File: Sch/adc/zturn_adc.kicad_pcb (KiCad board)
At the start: 4 copper layers, 91.5 x 80 mm, 118 parts, among them CN1 SMA, CN2 SMA, CN3 AudioJack, J1 JP4, J2 Header5, J3 JP2, J4 JP2, J5 JP2, J6 JP2, P1 CONN_02X40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

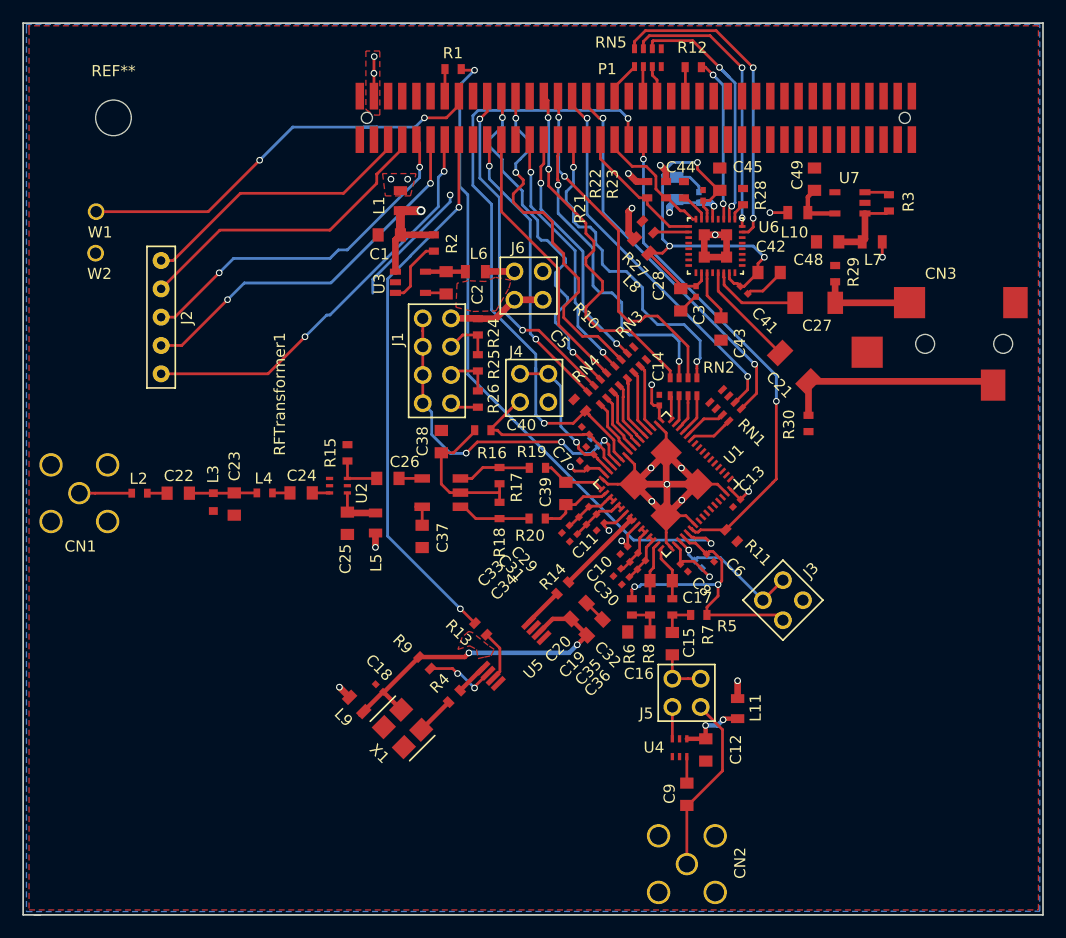
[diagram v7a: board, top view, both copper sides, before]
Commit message: Modify footprint to include 1-pin indicator. Routing almost done.
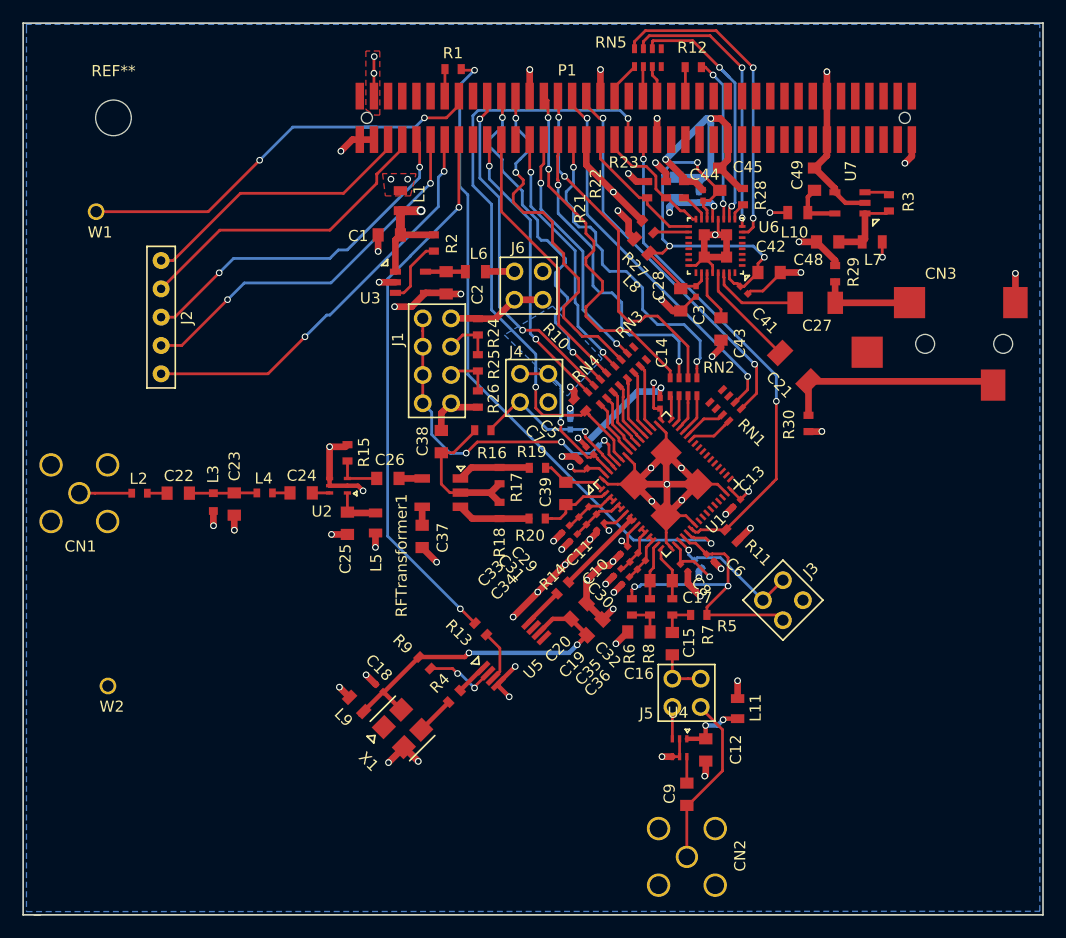
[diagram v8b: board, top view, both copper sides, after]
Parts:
- C40: moved to B.Cu
- moved W2 38.8 mm to (93.6, 114.5)
- moved C40 1.49 mm to (135.1, 91.0), turned to 90 degrees
- moved CN2 0.65 mm to (145.6, 129.8)
- moved C14 0.29 mm to (143.1, 89.1)
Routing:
- net GND: track 70.1 -> 237.6 mm, vias 6 -> 60
- net (no net): track 11.7 -> 0.00 mm, vias 1 -> 0
- net /RF_in/VCMA: track 16.6 -> 14.8 mm, vias 0 -> 1
- net /RF_in/VCMB: track 25.1 -> 26.8 mm
- net /CN/SHDNA: track 56.9 -> 55.9 mm
- net Net-(C9-Pad2): track 16.3 -> 15.6 mm
- net Net-(C37-Pad1): track 2.26 -> 1.66 mm
- removed copper zone on F.Cu, net GND
